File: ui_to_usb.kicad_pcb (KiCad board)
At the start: 2 copper layers, 39.2 x 29 mm, 43 parts, among them J1 TYPE-C-31-M-12, J2 PM254-2-06-S-8.5, J3 BM12B-SRSS-TB, SW1 BOOT0, SW2 RST, U1 SPX3819M5-L, U2 USBLC6-2SC6, U3 CH32V203K8T6, Y1 8M

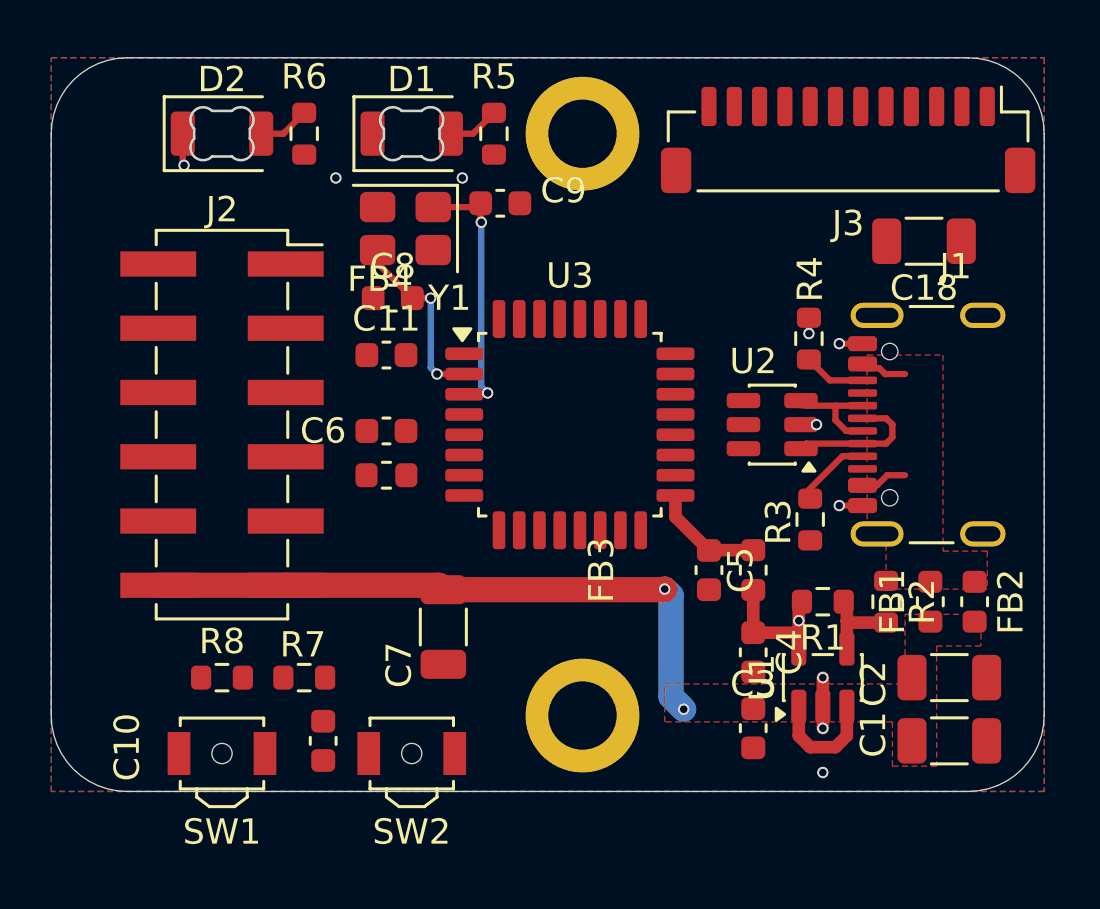
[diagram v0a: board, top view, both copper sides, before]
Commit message: switch to 4 layers, all traces routed
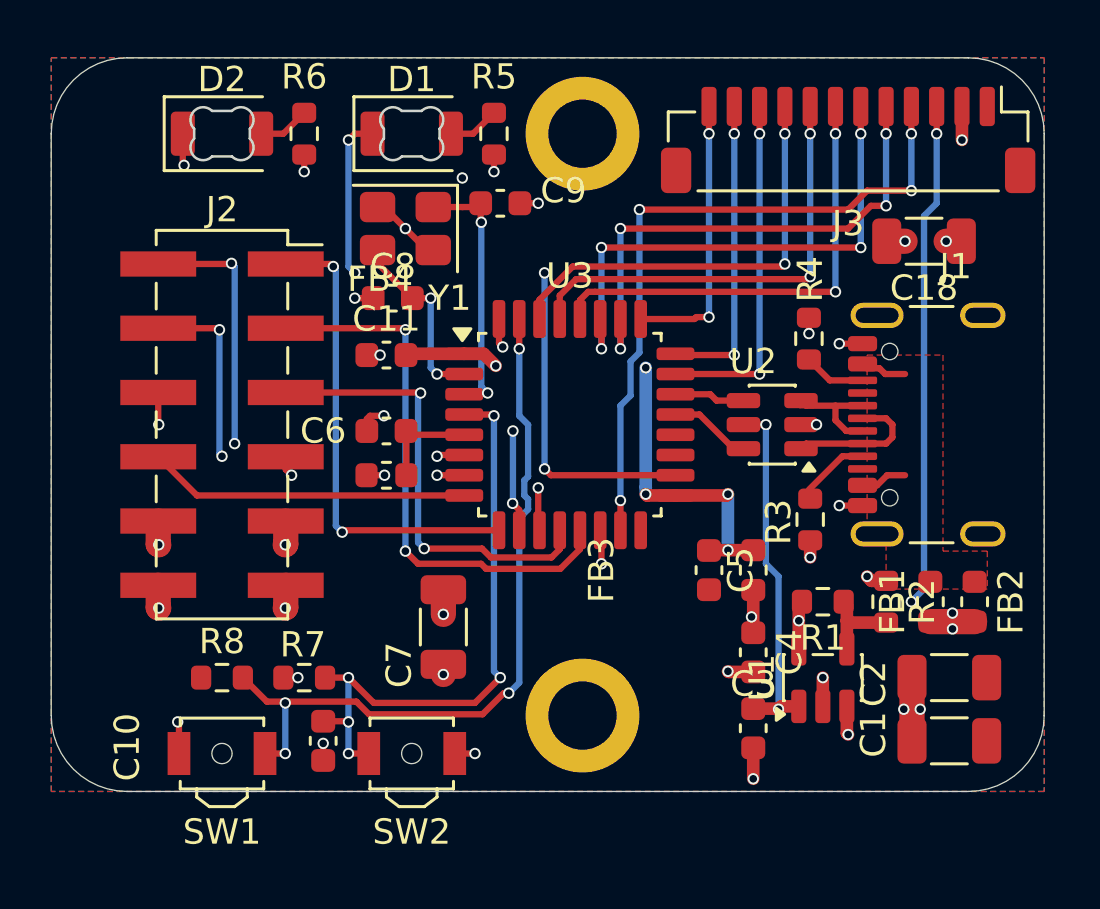
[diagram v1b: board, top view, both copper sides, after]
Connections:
- R5 pad 2: +3.3V -> +3V3
- R6 pad 2: +3.3V -> +3V3
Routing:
- net /PB0: track 0.00 -> 34.2 mm, vias 0 -> 3
- net /BOOT0: track 0.00 -> 29.6 mm, vias 0 -> 4
- net /PB1: track 0.00 -> 27.4 mm, vias 0 -> 4
- net Net-(D1-K): track 0.00 -> 26.9 mm, vias 0 -> 4
- net /RST_N: track 0.00 -> 24.2 mm, vias 0 -> 5
- net /SDO: track 0.00 -> 21.8 mm, vias 0 -> 2
- net /PB4: track 0.00 -> 21.0 mm, vias 0 -> 4
- net /PB3: track 0.00 -> 20.7 mm, vias 0 -> 4
- net /CS_IO_N: track 0.00 -> 19.4 mm, vias 0 -> 3
- net /INT_IO: track 0.00 -> 19.4 mm, vias 0 -> 3
- net /CS_OLED_N: track 0.00 -> 18.8 mm, vias 0 -> 2
- net /PB5: track 0.00 -> 18.3 mm, vias 0 -> 2
- net /SDI: track 0.00 -> 18.0 mm, vias 0 -> 2
- net /PB6: track 0.00 -> 17.9 mm, vias 0 -> 2
- net VDD: track 4.48 -> 22.0 mm, vias 0 -> 5
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- added copper zone on In1.Cu, net +3V3
- added copper zone on In1.Cu, net +5V
- removed copper zone on F.Cu, net +5V
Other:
- copper layers 2 -> 4

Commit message: add tactile button footprint
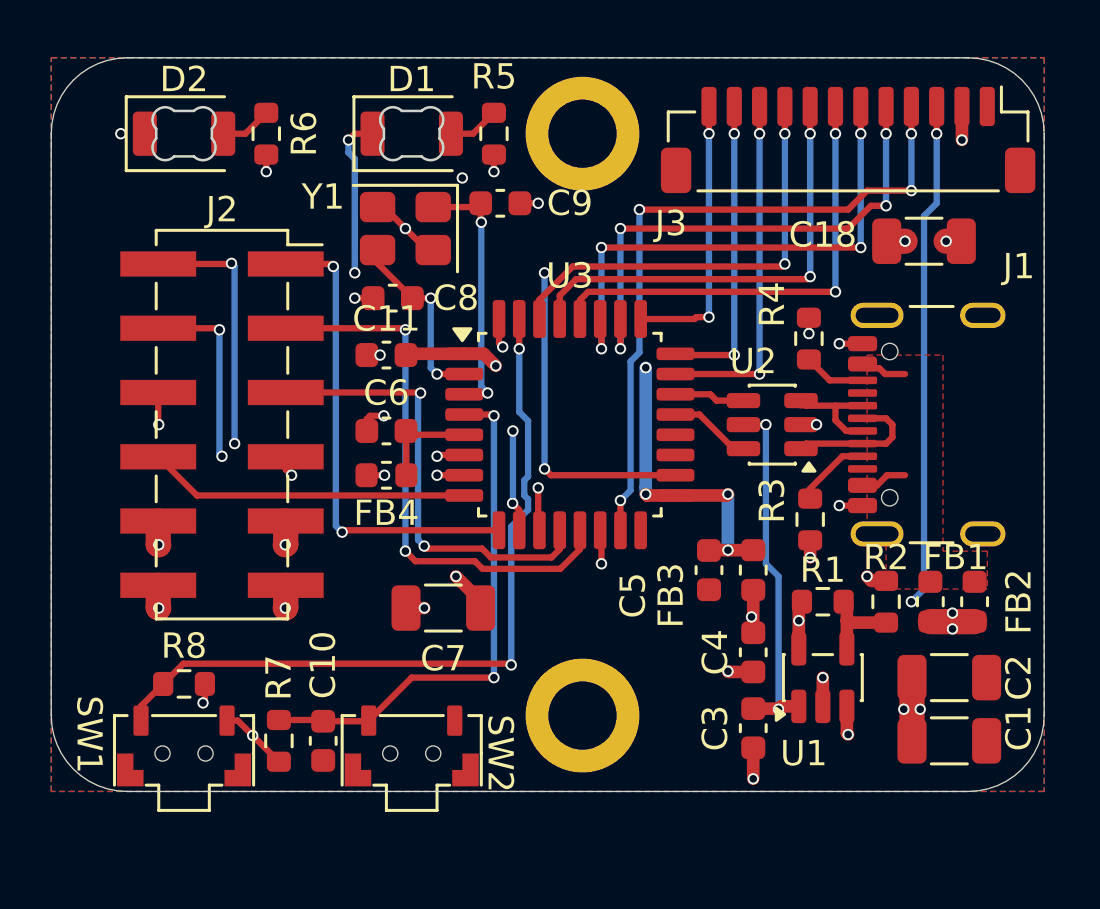
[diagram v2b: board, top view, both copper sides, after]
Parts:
- SW1: value BOOT0 -> TS24CA; footprint Button_Switch_SMD:SW_SPST_B3U-3000P-B -> footprints:TS24CA
- SW2: value RST -> TS24CA; footprint Button_Switch_SMD:SW_SPST_B3U-3000P-B -> footprints:TS24CA
- moved R7 2.69 mm to (83.3, 92.5), turned to -90 degrees
- moved R8 1.52 mm to (79.5, 90.3), turned to 180 degrees
- moved D2 1.50 mm to (79.5, 68.5)
- moved R6 1.50 mm to (82.8, 68.5)
- moved SW1 1.50 mm to (79.5, 93.0)
- moved C7 0.75 mm to (89.8, 87.3), turned to 180 degrees
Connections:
- SW1 pad 1: /BOOT0 -> +3V3
- SW1 pad 2: +3V3 -> /BOOT0
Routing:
- net /RST_N: track 24.2 -> 20.8 mm, vias 5 -> 2
- net +3V3: track 9.43 -> 10.3 mm, vias 9 -> 8
- net GND: track 21.0 -> 20.2 mm, vias 23 -> 22
- net /BOOT0: track 29.6 -> 30.1 mm, vias 4 -> 2
- added copper zone on In2.Cu, net GND

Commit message: layout looks decent, 0 DRC errors
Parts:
- moved kibuzzard-6951C425 0.78 mm to (79.5, 71.1)
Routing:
- net /PB0: track 34.2 -> 30.8 mm, vias 3 -> 4
- net +3V3: track 10.3 -> 11.4 mm
- net Net-(D1-K): track 26.9 -> 26.3 mm
- net GND: track 20.2 -> 20.6 mm, vias 22 -> 31
- added copper zone on In2.Cu, net +3V3
- added copper zone on In2.Cu, net +5V
- added copper zone on In1.Cu, net GND
- removed copper zone on In1.Cu, net +3V3
- removed copper zone on In1.Cu, net +5V
- removed copper zone on In2.Cu, net GND

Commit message: Layout looks decent. Ready to order.
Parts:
- removed the G*** at (85.2, 88.4)
- removed the G*** at (92.3, 75.6)
- added A10: U_RX, TestPoint:TestPoint_Pad_D1.0mm, F.Cu at (102.0, 82.4)
- added A9: U_TX, TestPoint:TestPoint_Pad_D1.0mm, F.Cu at (100.6, 83.5)
- added G***: LOGO, LOGO, B.Cu at (93.6, 73.1)
- added G***: LOGO, LOGO, B.Cu at (82.5, 86.3)
- moved G1 14.5 mm to (108.3, 80.0)
- moved G2 8.55 mm to (94.5, 83.4)
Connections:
- U3 pad 19: unconnected-(U3-PA9-Pad19) -> Net-(U3-PA9)
- U3 pad 20: unconnected-(U3-PA10-Pad20) -> Net-(U3-PA10)
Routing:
- net Net-(U3-PA10): track 0.00 -> 3.90 mm
- net Net-(U3-PA9): track 0.00 -> 3.43 mm
- net VDD: track 21.9 -> 23.4 mm, vias 5 -> 4
- net GND: track 20.6 -> 21.6 mm, vias 31 -> 32
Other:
- board text added: "A10"
- board text added: "A9"
- board text added: "B"
- board text added: "R"
- board text added: "betz-engineering.ch/open_hardware/ui_to_usb/"
- board text removed: "https://github.com/betz-engineering/ui_to_usb"

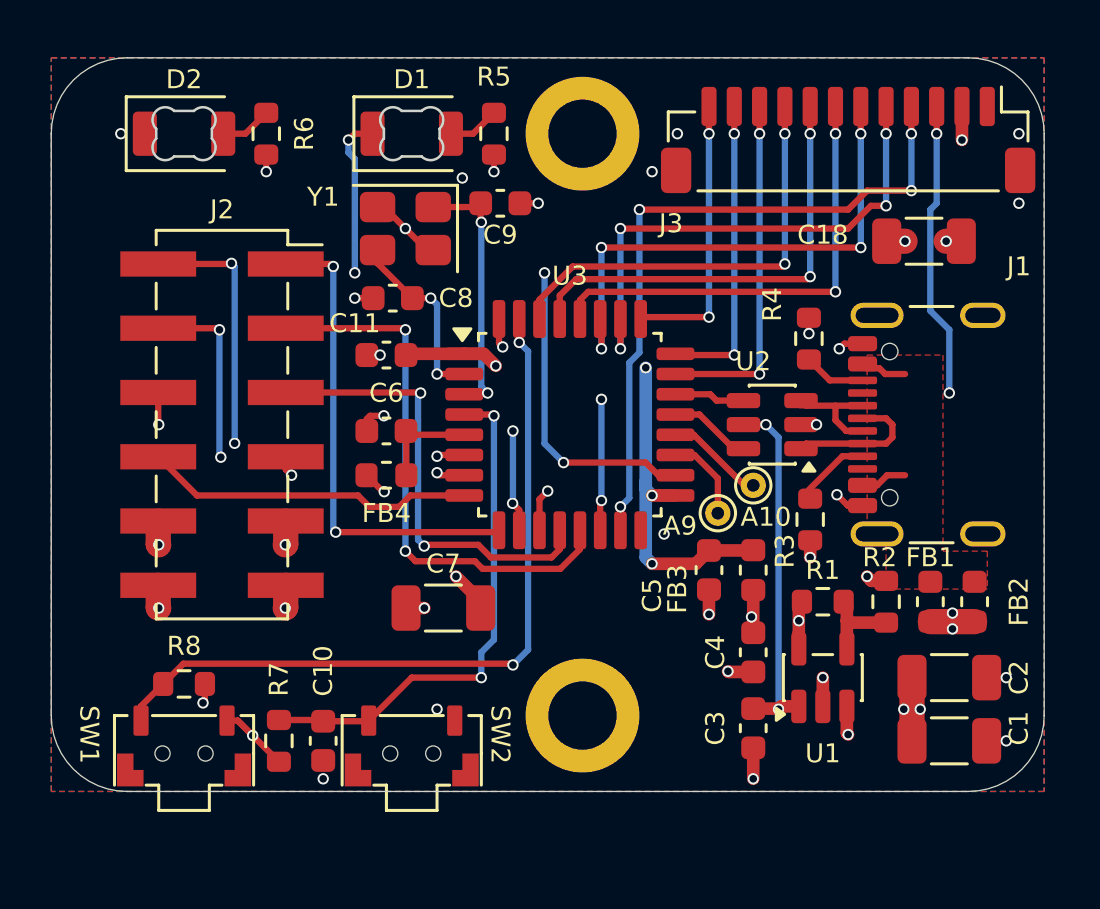
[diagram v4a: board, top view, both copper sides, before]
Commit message: moved tactile buttons because of colission with shroud on ui_board_1u
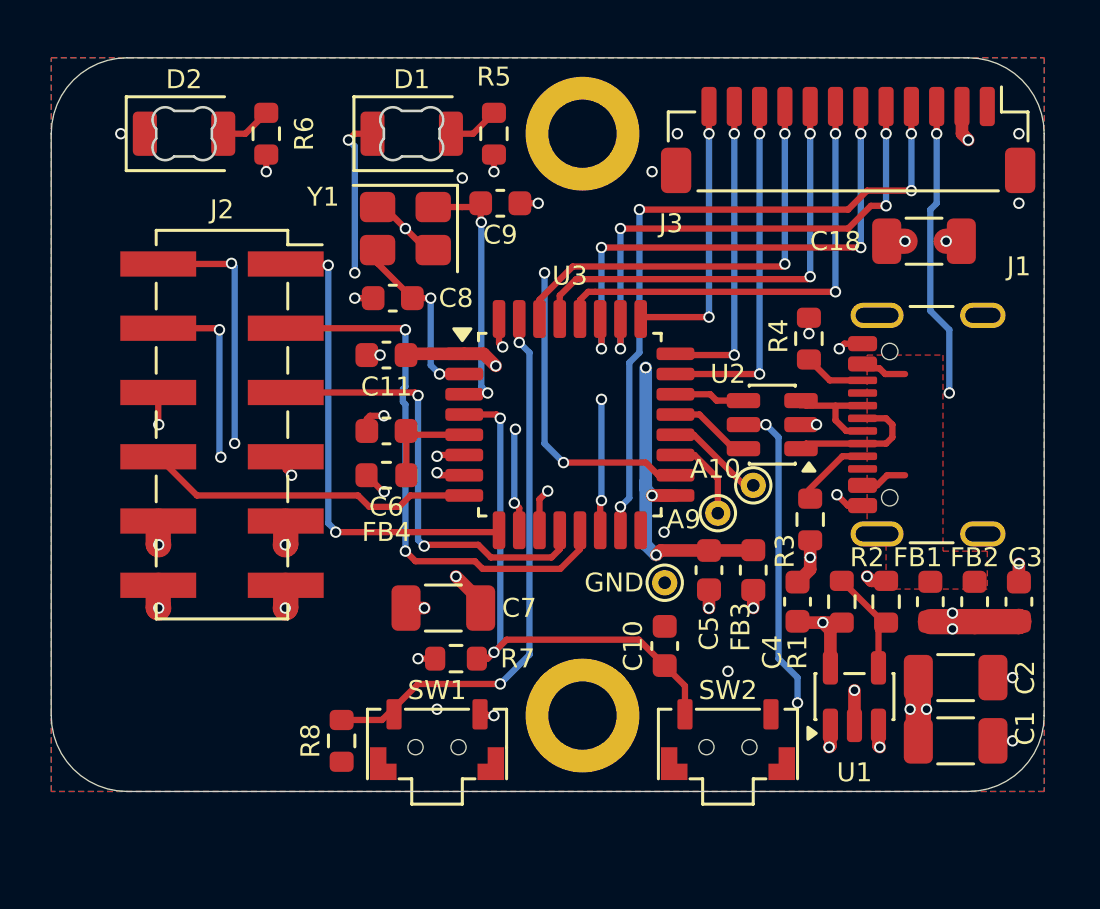
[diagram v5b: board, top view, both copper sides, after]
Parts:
- added TP3: GND, TestPoint:TestPoint_Pad_D1.0mm, F.Cu at (98.5, 86.3)
- added kibuzzard-698F1642: G***, kibuzzard-698F1642, B.Cu at (101.0, 93.7)
- added kibuzzard-698F164A: G***, kibuzzard-698F164A, B.Cu at (89.4, 93.7)
- TP1: renamed from A9; value U_TX -> A9
- TP2: renamed from A10; value U_RX -> A10
- moved C10 14.0 mm to (98.5, 88.8), turned to -90 degrees
- moved SW2 12.5 mm to (101.0, 92.8)
- moved C3 11.6 mm to (112.5, 87.0), turned to -90 degrees
- moved SW1 10.0 mm to (89.5, 92.8)
- moved R7 7.72 mm to (90.3, 89.3), turned to 180 degrees
- moved R8 6.62 mm to (85.7, 92.5), turned to 90 degrees
- moved C4 2.66 mm to (103.8, 87.0), turned to 90 degrees
- moved U1 1.46 mm to (106.0, 90.8)
- moved G2 1.39 mm to (95.8, 83.1)
- moved R1 0.75 mm to (105.5, 87.0), turned to -90 degrees
- moved kibuzzard-6951C425 0.31 mm to (79.5, 70.7)
- moved kibuzzard-6951C42C 0.31 mm to (88.5, 70.7)
- moved C1 0.25 mm to (110.0, 92.5)
- moved C2 0.25 mm to (110.0, 90.0)
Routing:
- net /BOOT0: track 30.1 -> 21.9 mm
- net +3V3: track 11.4 -> 10.1 mm, vias 8 -> 9
- net GND: track 21.6 -> 20.5 mm, vias 32 -> 30
- net Net-(U1-ADJ): track 3.50 -> 4.35 mm
- net +5V: track 22.1 -> 22.7 mm, vias 10 -> 11
- net VDD: track 23.4 -> 22.8 mm
- net /RST_N: track 20.5 -> 21.0 mm
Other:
- board text added: "GND"
- board text removed: "B"
- board text removed: "R"

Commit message: change 3V3 feedback resistor for more common values
sent for production
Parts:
- R1: value 37k4 -> 30k
- R2: value 22k -> 18k
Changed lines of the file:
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@@
 			)
 		)
-		(property "Value" "37k4"
+		(property "Value" "30k"
 			(at 0 1.43 90)
 			(layer "F.Fab")
@@
 			)
 		)
-		(property "Value" "22k"
+		(property "Value" "18k"
 			(at 0 1.43 90)
 			(layer "F.Fab")
